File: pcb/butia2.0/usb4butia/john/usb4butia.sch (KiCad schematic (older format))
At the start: 48 parts, among them J1 USB_B, J2 RJ45, J3 RJ45, J4 RJ45, J5 RJ45, J6 RJ45, J7 RJ45, K1 AX-12, K2 V_5_10, K3 CONN_3, P1 PICkit2, P2 CONN_2X2, P3 CONN_2, P4 CONN_2, P5 CONN_4, P6 CONN_1, P7 CONN_1, P8 CONN_1, SW1 RST, SW2 PROG, U1 PIC18F4550, X1 20MHz, X2 32.768KHz

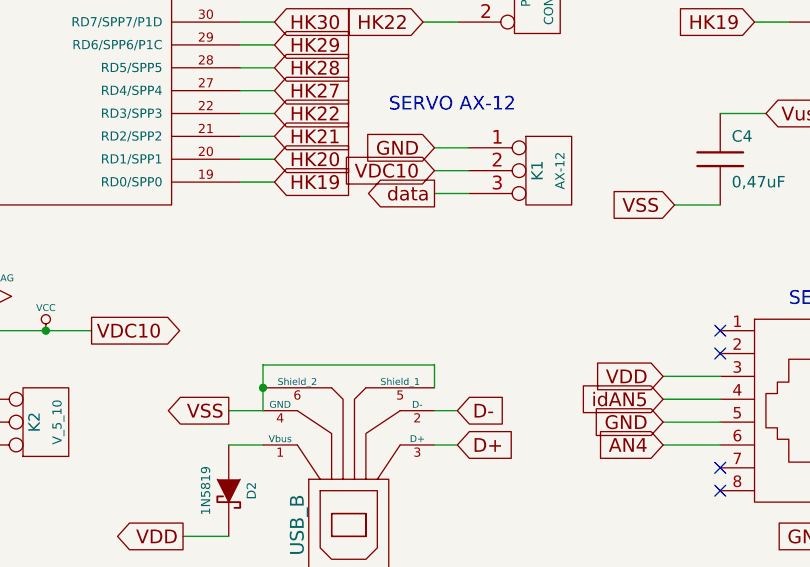
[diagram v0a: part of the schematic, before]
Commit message: Change dicrection and add pull up for AX12 conector, v1.6
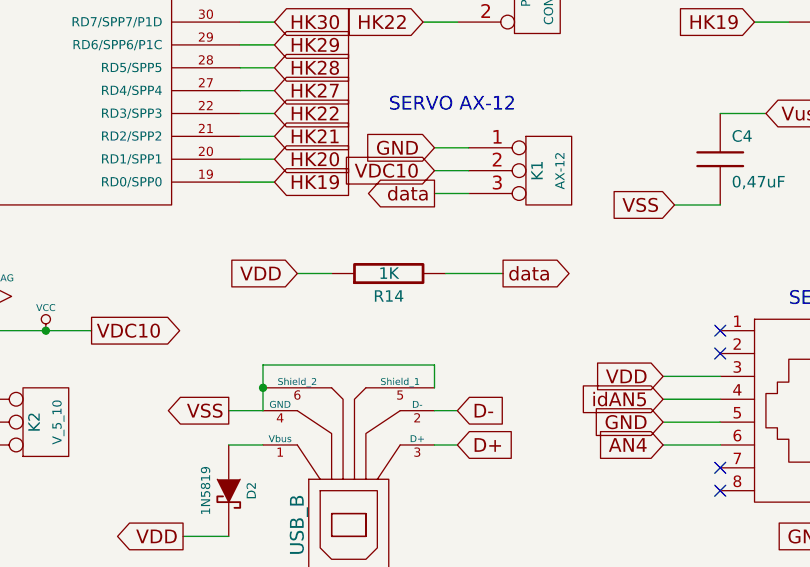
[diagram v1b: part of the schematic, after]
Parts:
- added R14: 1K, symbol R
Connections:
- net +5V: now also R14.1
- net data: now also R14.2

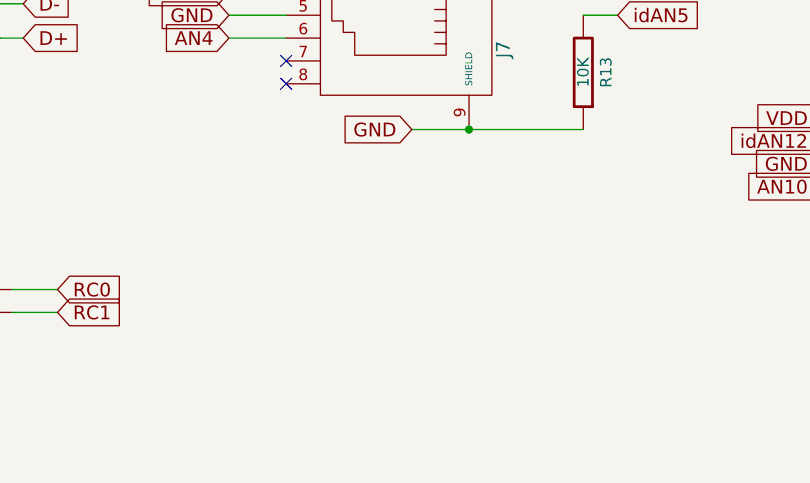
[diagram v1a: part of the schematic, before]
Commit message: Formalizate Bridges definition usb4butia1.7.3
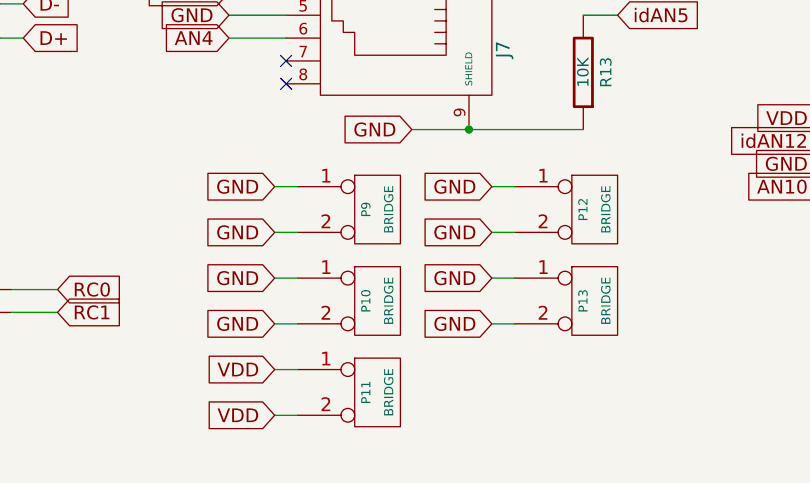
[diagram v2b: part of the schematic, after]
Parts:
- added P10, P11, P12, P13, P9: BRIDGE, symbol CONN_2
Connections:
- net +5V: now also P11.1 (P1), P11.2 (PM)
- net GND: now also P10.1 (P1), P10.2 (PM), P12.1 (P1), P12.2 (PM), P13.1 (P1), P13.2 (PM), P9.1 (P1), P9.2 (PM)
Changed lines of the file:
@@
-EESchema Schematic File Version 2  date vie 20 abr 2012 20:55:54 UYT
+EESchema Schematic File Version 2  date mié 06 jun 2012 23:04:25 UYT
 LIBS:power
 LIBS:device
@@
 Sheet 1 1
 Title "USB4butia"
-Date "20 apr 2012"
+Date "7 jun 2012"
 Rev "1.0"
 Comp ""
@@
 Comment4 ""
 $EndDescr
+Text GLabel 6200 7300 0    60   Input ~ 0
+VDD
+Text GLabel 6200 7100 0    60   Input ~ 0
+VDD
+Wire Wire Line
+	6200 7300 6300 7300
+Wire Wire Line
+	6200 7100 6300 7100
+$Comp
+L CONN_2 P11
+U 1 1 4FD00BFB
+P 6650 7200
+F 0 "P11" V 6600 7200 40  0000 C CNN
+F 1 "BRIDGE" V 6700 7200 40  0000 C CNN
+	1    6650 7200
+	1    0    0    -1
+$EndComp
+$Comp
+L CONN_2 P10
+U 1 1 4FD00BAA
+P 6650 6800
+F 0 "P10" V 6600 6800 40  0000 C CNN
+F 1 "BRIDGE" V 6700 6800 40  0000 C CNN
+	1    6650 6800
+	1    0    0    -1
+$EndComp
+Text GLabel 6200 6700 0    60   Input ~ 0
+GND
+Text GLabel 6200 6900 0    60   Input ~ 0
+GND
+Wire Wire Line
+	6200 6700 6300 6700
+Wire Wire Line
+	6200 6900 6300 6900
+Wire Wire Line
+	7150 6900 7250 6900
+Wire Wire Line
+	7150 6700 7250 6700
+Text GLabel 7150 6900 0    60   Input ~ 0
+GND
+Text GLabel 7150 6700 0    60   Input ~ 0
+GND
+$Comp
+L CONN_2 P13
+U 1 1 4FD00BA9
+P 7600 6800
+F 0 "P13" V 7550 6800 40  0000 C CNN
+F 1 "BRIDGE" V 7650 6800 40  0000 C CNN
+	1    7600 6800
+	1    0    0    -1
+$EndComp
+$Comp
+L CONN_2 P12
+U 1 1 4FD00B9E
+P 7600 6400
+F 0 "P12" V 7550 6400 40  0000 C CNN
+F 1 "BRIDGE" V 7650 6400 40  0000 C CNN
+	1    7600 6400
+	1    0    0    -1
+$EndComp
+Text GLabel 7150 6300 0    60   Input ~ 0
+GND
+Text GLabel 7150 6500 0    60   Input ~ 0
+GND
+Wire Wire Line
+	7150 6300 7250 6300
+Wire Wire Line
+	7150 6500 7250 6500
+Wire Wire Line
+	6200 6500 6300 6500
 Wire Wire Line
 	5300 4900 5050 4900
@@
 Wire Wire Line
 	4400 4900 4550 4900
+Wire Wire Line
+	6200 6300 6300 6300
+Text GLabel 6200 6500 0    60   Input ~ 0
+GND
+Text GLabel 6200 6300 0    60   Input ~ 0
+GND
+$Comp
+L CONN_2 P9
+U 1 1 4FD00A52
+P 6650 6400
+F 0 "P9" V 6600 6400 40  0000 C CNN
+F 1 "BRIDGE" V 6700 6400 40  0000 C CNN
+	1    6650 6400
+	1    0    0    -1
+$EndComp
 Text GLabel 5300 4900 2    60   Output ~ 0
 data

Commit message: Still working in usb4buti 1.7.4
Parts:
- removed K2: V_5_10, symbol CONN_3
- added P14: CONN_2, symbol CONN_2
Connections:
- net GND: now also P14.2 (PM)
- net VCC: now also P14.1 (P1)

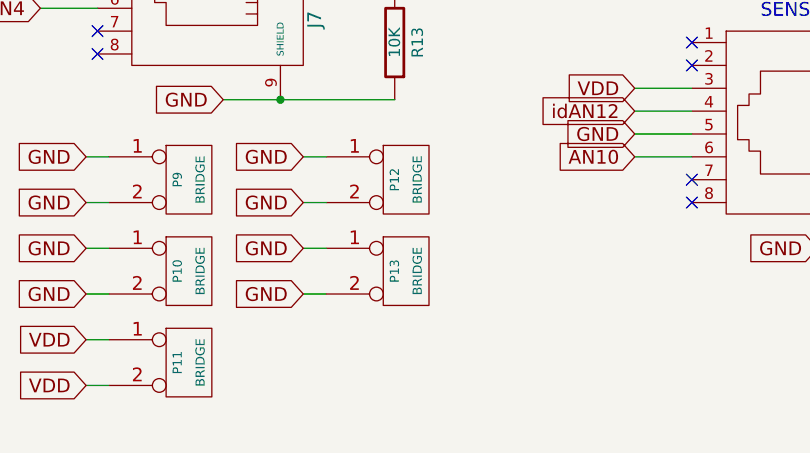
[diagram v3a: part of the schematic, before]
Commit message: usb4butia1.8 have bornier for switch
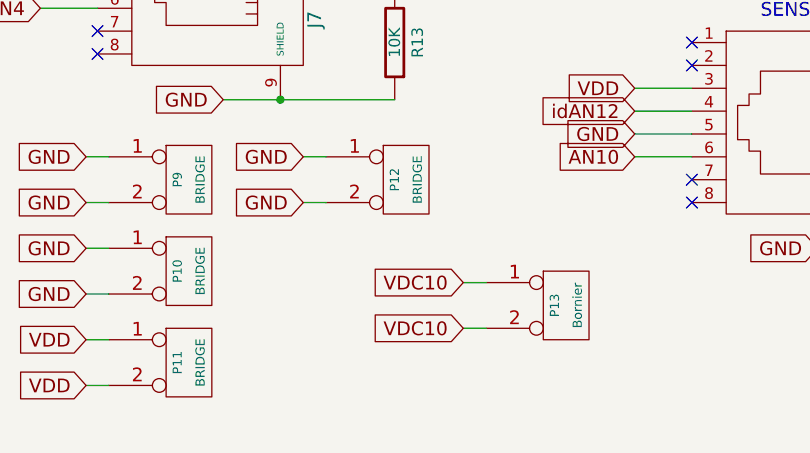
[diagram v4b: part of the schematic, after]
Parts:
- P13: value BRIDGE -> Bornier
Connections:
- net GND: no longer P13.1 (P1), P13.2 (PM)
- net VCC: now also P13.1 (P1), P13.2 (PM)
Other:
- moved on the sheet: P13
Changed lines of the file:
@@
-EESchema Schematic File Version 2  date vie 08 jun 2012 09:19:17 UYT
+EESchema Schematic File Version 2  date lun 11 jun 2012 15:14:07 UYT
 LIBS:power
 LIBS:device
@@
 Sheet 1 1
 Title "USB4butia"
-Date "8 jun 2012"
+Date "11 jun 2012"
 Rev "1.0"
 Comp ""
@@
 Comment4 ""
 $EndDescr
+Text GLabel 7850 7050 0    60   Input ~ 0
+VDC10
+Text GLabel 7850 6850 0    60   Input ~ 0
+VDC10
 Text GLabel 3250 4800 2    60   Input ~ 0
 VDD
@@
 	7150 6300 7250 6300
 Wire Wire Line
-	7150 6700 7250 6700
-Wire Wire Line
-	7150 6900 7250 6900
+	7850 6850 7950 6850
+Wire Wire Line
+	7850 7050 7950 7050
 Wire Wire Line
 	6200 6900 6300 6900
@@
 Text GLabel 6200 6900 0    60   Input ~ 0
 GND
-Text GLabel 7150 6900 0    60   Input ~ 0
-GND
-Text GLabel 7150 6700 0    60   Input ~ 0
-GND
 $Comp
 L CONN_2 P13
 U 1 1 4FD00BA9
-P 7600 6800
-F 0 "P13" V 7550 6800 40  0000 C CNN
-F 1 "BRIDGE" V 7650 6800 40  0000 C CNN
-	1    7600 6800
+P 8300 6950
+F 0 "P13" V 8250 6950 40  0000 C CNN
+F 1 "Bornier" V 8350 6950 40  0000 C CNN
+	1    8300 6950
 	1    0    0    -1
 $EndComp

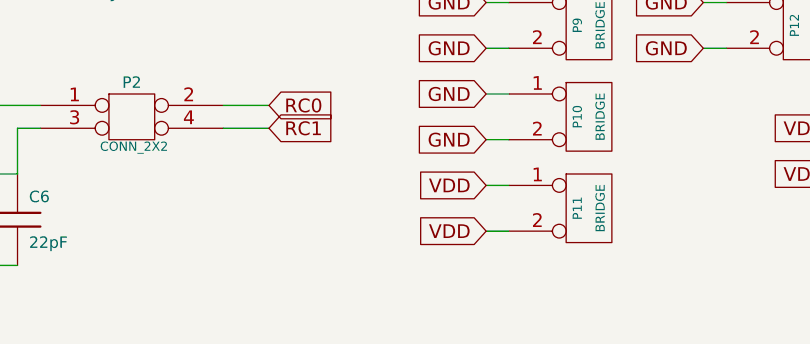
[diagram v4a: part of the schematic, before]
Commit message: Fix somes bridge problems and replce jack connector usb4butia 1.8.1
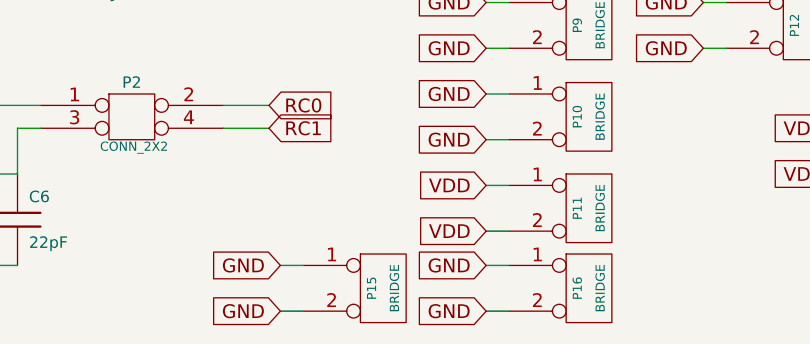
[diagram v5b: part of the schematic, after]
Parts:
- added P15, P16: BRIDGE, symbol CONN_2
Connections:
- net GND: now also P15.1 (P1), P15.2 (PM), P16.1 (P1), P16.2 (PM)
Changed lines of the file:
@@
-EESchema Schematic File Version 2  date lun 11 jun 2012 15:14:07 UYT
+EESchema Schematic File Version 2  date mié 20 jun 2012 10:02:24 UYT
 LIBS:power
 LIBS:device
@@
 Sheet 1 1
 Title "USB4butia"
-Date "11 jun 2012"
+Date "20 jun 2012"
 Rev "1.0"
 Comp ""
@@
 Comment4 ""
 $EndDescr
+Wire Wire Line
+	5300 7450 5400 7450
+Wire Wire Line
+	5300 7650 5400 7650
+Text GLabel 5300 7650 0    60   Input ~ 0
+GND
+Text GLabel 5300 7450 0    60   Input ~ 0
+GND
+$Comp
+L CONN_2 P15
+U 1 1 4FE1C3F9
+P 5750 7550
+F 0 "P15" V 5700 7550 40  0000 C CNN
+F 1 "BRIDGE" V 5800 7550 40  0000 C CNN
+	1    5750 7550
+	1    0    0    -1
+$EndComp
+$Comp
+L CONN_2 P16
+U 1 1 4FE1C3E9
+P 6650 7550
+F 0 "P16" V 6600 7550 40  0000 C CNN
+F 1 "BRIDGE" V 6700 7550 40  0000 C CNN
+	1    6650 7550
+	1    0    0    -1
+$EndComp
+Text GLabel 6200 7450 0    60   Input ~ 0
+GND
+Text GLabel 6200 7650 0    60   Input ~ 0
+GND
+Wire Wire Line
+	6200 7650 6300 7650
+Wire Wire Line
+	6200 7450 6300 7450
 Text GLabel 7850 7050 0    60   Input ~ 0
 VDC10
